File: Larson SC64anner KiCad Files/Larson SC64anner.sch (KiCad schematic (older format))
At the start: 67 parts, among them J1 Conn_02x03_Counter_Clockwise, J10 Conn_02x03_Counter_Clockwise, J11 Conn_02x03_Counter_Clockwise, J12 Conn_02x03_Counter_Clockwise, J13 Conn_02x03_Counter_Clockwise, J14 Conn_02x03_Counter_Clockwise, J15 Conn_02x03_Counter_Clockwise, J16 Conn_02x03_Counter_Clockwise, J17 Conn_02x03_Counter_Clockwise, J18 Conn_02x03_Counter_Clockwise, J19 Conn_02x03_Counter_Clockwise, J2 Conn_02x03_Counter_Clockwise, J20 Conn_02x03_Counter_Clockwise, J21 Conn_01x02, J3 Conn_02x03_Counter_Clockwise, J4 Conn_02x03_Counter_Clockwise, J5 Conn_02x03_Counter_Clockwise, J6 Conn_02x03_Counter_Clockwise, J7 Conn_02x03_Counter_Clockwise, J8 Conn_02x03_Counter_Clockwise, J9 Conn_02x03_Counter_Clockwise, U1 ATtiny85V-10PU

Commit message: no message
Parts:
- added C1, C2, C3: 10uF, Capacitor_THT:CP_Radial_D5.0mm_P2.50mm, symbol Device:CP
- added C4: 10nF, Capacitor_THT:C_Disc_D7.5mm_W2.5mm_P5.00mm, symbol Device:C
- added D1: 1N4148, Diode_THT:D_DO-35_SOD27_P7.62mm_Horizontal, symbol Diode:1N4148
- added J22, J27: 1x02, Connector_PinHeader_2.54mm:PinHeader_1x02_P2.54mm_Vertical, symbol Connector_Generic:Conn_01x02
- added J23, J24, J25, J26: 1x01, Connector_PinHeader_2.54mm:PinHeader_1x01_P2.54mm_Vertical, symbol Connector:Conn_01x01_Male
- added R26, R27: 10k Ohm, Resistor_THT:R_Axial_DIN0207_L6.3mm_D2.5mm_P2.54mm_Vertical, symbol Device:R
- added R28: 150 Ohm, Resistor_THT:R_Axial_DIN0207_L6.3mm_D2.5mm_P2.54mm_Vertical, symbol Device:R
- added R29: 10k Ohm linear, Connector_PinHeader_2.54mm:PinHeader_1x03_P2.54mm_Vertical, symbol Device:R_POT
- added U2: NE555, Package_DIP:DIP-8_W7.62mm, symbol Timer:NE555
- added U3: SN74LVC2GU04DCKR, https://www.ti.com/lit/ds/symlink/sn74lvc2gu04.pdf, symbol dk_Logic-Buffers-Drivers-Receivers-Transceivers:SN74LVC2G17DBVR_Discontinued
- J1, J10, J11, J12, J13, J14, J15, J16, J17, J18, J19, J2, J20, J3, J4, J5, J6, J7, J8, J9: value Conn_02x03_Counter_Clockwise -> 2x03; Category (none) -> Pin Header; DK_Datasheet_Link (none) -> https://www.digikey.de/product-detail/en/amphenol-icc-fci/6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; DK_Product_Page (none) -> https://www.digikey.de/product-detail/en/amphenol-icc-fci/6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; Family (none) -> LSC; Price (none) -> 0,3
- J21: value Conn_01x02 -> 1x02; Category (none) -> Pin Header; DK_Datasheet_Link (none) -> https://www.digikey.de/product-detail/en/te-connectivity-am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; DK_Product_Page (none) -> https://www.digikey.de/product-detail/en/te-connectivity-am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; Family (none) -> LSC; Price (none) -> 0,55
- LED1, LED10, LED11, LED12, LED13, LED14, LED15, LED16, LED17, LED18, LED19, LED2, LED20, LED3, LED4, LED5, LED6, LED7, LED8, LED9: Category (none) -> LED; DK_Datasheet_Link (none) -> https://www.digikey.de/product-detail/de/kingbright/WP154A4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; DK_Product_Page (none) -> https://www.digikey.de/product-detail/de/kingbright/WP154A4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; Family (none) -> LSC; Price (none) -> 1,74
- R1, R10, R11, R12, R13, R14, R15, R16, R17, R18, R19, R2, R20, R3, R4, R5, R6, R7, R8, R9: value 80 -> 80 Ohm; Category (none) -> Resistor; DK_Datasheet_Link (none) -> https://www.digikey.de/product-detail/en/vishay-dale/CMF608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; DK_Product_Page (none) -> https://www.digikey.de/product-detail/en/vishay-dale/CMF608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; Family (none) -> LSC; Price (none) -> 0,73
- R21, R22, R23, R24, R25: value 10 -> 10 Ohm; Category (none) -> Resistor; DK_Datasheet_Link (none) -> https://www.digikey.de/product-detail/en/bourns-inc/FW10A10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; DK_Product_Page (none) -> https://www.digikey.de/product-detail/en/bourns-inc/FW10A10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; Family (none) -> LSC; Price (none) -> 0,53
- U1: value ATtiny85V-10PU -> ATtiny85V-20PU; symbol MCU_Microchip_ATtiny:ATtiny85V-10PU -> MCU_Microchip_ATtiny:ATtiny85-20PU; Category (none) -> IC; DK_Datasheet_Link (none) -> https://www.digikey.com/product-detail/en/microchip-technol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; DK_Product_Page (none) -> https://www.digikey.de/product-detail/de/microchip-technolo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; Family (none) -> LSC; Price (none) -> 1,10
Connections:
- new net: C1.1, J22.1 (Pin_1), R26.2
- new net: C2.1, J22.2 (Pin_2), R27.2
- new net: C1.2, D1.1 (K), J23.1 (Pin_1), R26.1
- new net: C2.2, D1.2 (A), R27.1
- new net: R28.1, R29.1, R29.2, U2.7 (DIS)
- new net: J27.2 (Pin_2), R29.3, U2.4 (R), U2.8 (VCC), U3.5 (VCC)
- new net: C3.1, R28.2, U2.2 (TR), U2.6 (THR)
- new net: C3.2, C4.2, J25.1 (Pin_1), U2.1 (GND), U3.2 (GND)
- new net: U2.3 (Q), U3.1 (1A)
- new net: C4.1, U2.5 (CV)
- new net: U3.3 (2A), U3.6 (1Y)
- new net: J26.1 (Pin_1), U3.4 (2Y)
- new net: J24.1 (Pin_1), J27.1 (Pin_1)

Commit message: Add files via upload
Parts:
- removed J25: 1x01, Connector_PinHeader_2.54mm:PinHeader_1x01_P2.54mm_Vertical, symbol Connector:Conn_01x01_Male
- removed J27: 1x02, Connector_PinHeader_2.54mm:PinHeader_1x02_P2.54mm_Vertical, symbol Connector_Generic:Conn_01x02
- added J26: 1x01, Connector_PinHeader_2.54mm:PinHeader_1x01_P2.54mm_Vertical, symbol Connector:Conn_01x01_Male
- renumbered J26 to J25
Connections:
- net at R28.1, R29.2, U2.7 (DIS): now also R29.3; no longer R29.1
- net at U2.4 (R), U2.8 (VCC), U3.5 (VCC): now also J24.1 (Pin_1), R29.1; no longer R29.3
- net at C3.1, R28.2, U2.2 (TR)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: now also J26.1 (Pin_1)
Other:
- moved on the sheet: R29
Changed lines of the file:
@@
 F 8 "CPU Brake" H 20300 2050 50  0001 C CNN "Family"
 	1    20300 2050
-	0    1    1    0
+	0    -1   -1   0
 $EndComp
 $Comp
@@
 $EndComp
 $Comp
-L Connector:Conn_01x01_Male J26
+L Connector:Conn_01x01_Male J25
 U 1 1 5EA768C3
 P 18900 5150
-F 0 "J26" H 19008 5331 50  0000 C CNN
+F 0 "J25" H 19008 5331 50  0000 C CNN
 F 1 "1x01" H 19000 5250 50  0000 C CNN
 F 2 "Connector_PinHeader_2.54mm:PinHeader_1x01_P2.54mm_Vertical" H 18900 5150 50  0001 C CNN
@@
 $EndComp
 $Comp
-L Connector:Conn_01x01_Male J25
-U 1 1 5EAA3C5C
-P 22200 4500
-F 0 "J25" H 22308 4681 50  0000 C CNN
-F 1 "1x01" H 22300 4600 50  0000 C CNN
-F 2 "Connector_PinHeader_2.54mm:PinHeader_1x01_P2.54mm_Vertical" H 22200 4500 50  0001 C CNN
-F 3 "http://www.adam-tech.com/downloader.php?p=PH1-XX-UA.pdf" H 22200 4500 50  0001 C CNN
-F 4 "Pin Header" H 22200 4500 50  0001 C CNN "Category"
-F 5 "https://www.digikey.de/product-detail/en/adam-tech/PH1-01-UA/2057-PH1-01-UA-ND/9830231" H 22200 4500 50  0001 C CNN "DK_Datasheet_Link"
-F 6 "https://www.digikey.de/product-detail/en/adam-tech/PH1-01-UA/2057-PH1-01-UA-ND/9830231" H 22200 4500 50  0001 C CNN "DK_Product_Page"
-F 7 "0,09" H 22200 4500 50  0001 C CNN "Price"
-F 8 "CPU Brake" H 22200 4500 50  0001 C CNN "Family"
-	1    22200 4500
-	-1   0    0    1
-$EndComp
-$Comp
 L Device:C C4
 U 1 1 5EAB8B01
@@
 F 0 "C4" H 20415 4241 50  0000 L CNN
 F 1 "10nF" H 20415 4150 50  0000 L CNN
-F 2 "Capacitor_THT:C_Disc_D7.5mm_W2.5mm_P5.00mm" H 20415 4059 50  0000 L CNN
+F 2 "Capacitor_THT:C_Disc_D7.5mm_W2.5mm_P5.00mm" H 20415 4059 50  0001 L CNN
 F 3 "http://www.vishay.com/docs/28535/vy2series.pdf" H 20300 4150 50  0001 C CNN
 F 4 "https://www.digikey.de/product-detail/de/vishay-bc-components/VY2103M63Y5US63V0/BC2698-ND/2356836" H 20300 4150 50  0001 C CNN "DK_Datasheet_Link"
@@
 	1    0    0    -1
 $EndComp
-$Comp
-L Connector_Generic:Conn_01x02 J27
-U 1 1 5EAFC628
-P 18950 2350
-F 0 "J27" H 18868 2025 50  0000 C CNN
-F 1 "1x02" H 18868 2116 50  0001 C CNN
-F 2 "Connector_PinHeader_2.54mm:PinHeader_1x02_P2.54mm_Vertical" H 18950 2350 50  0001 C CNN
-F 3 "https://www.te.com/commerce/DocumentDelivery/DDEController?Action=srchrtrv&DocNm=146256&DocType=Customer+Drawing&DocLang=English" H 18950 2350 50  0001 C CNN
-F 4 "Pin Header" H 18950 2350 50  0001 C CNN "Category"
-F 5 "https://www.digikey.de/product-detail/en/te-connectivity-amp-connectors/5-146256-3/A121369-ND/1153559" H 18950 2350 50  0001 C CNN "DK_Datasheet_Link"
-F 6 "https://www.digikey.de/product-detail/en/te-connectivity-amp-connectors/5-146256-3/A121369-ND/1153559" H 18950 2350 50  0001 C CNN "DK_Product_Page"
-F 7 "0,55" H 18950 2350 50  0001 C CNN "Price"
-F 8 "CPU Brake" H 18950 2350 50  0001 C CNN "Family"
-	1    18950 2350
-	0    -1   -1   0
-$EndComp
-Wire Wire Line
-	18350 2600 18950 2600
-Wire Wire Line
-	18950 2600 18950 2550
-Wire Wire Line
-	19050 2550 19050 2600
-Wire Wire Line
-	19050 2600 19350 2600
 Wire Wire Line
 	19350 2600 19350 2050
 Wire Wire Line
 	19350 2050 20150 2050
-Wire Wire Line
-	20300 2200 20300 2250
 Wire Wire Line
 	20500 2350 20300 2350
@@
 Wire Wire Line
 	22300 5150 19100 5150
-Connection ~ 22000 4500
 Wire Wire Line
 	20450 2050 20500 2050
@@
 Wire Wire Line
 	20500 2250 20300 2250
-Connection ~ 20300 2250
 Wire Wire Line
 	20300 2250 20300 2350
@@
 	19700 3850 19700 3200
 Connection ~ 19700 3200
+Wire Wire Line
+	18350 2600 19350 2600
+Wire Wire Line
+	20300 1900 20500 1900
+Wire Wire Line
+	20500 1900 20500 2050
+Connection ~ 20500 2050
+$Comp
+L Connector:Conn_01x01_Male J26
+U 1 1 5E8C2806
+P 19250 4500
+F 0 "J26" H 19358 4681 50  0000 C CNN
+F 1 "1x01" H 19350 4600 50  0000 C CNN
+F 2 "Connector_PinHeader_2.54mm:PinHeader_1x01_P2.54mm_Vertical" H 19250 4500 50  0001 C CNN
+F 3 "http://www.adam-tech.com/downloader.php?p=PH1-XX-UA.pdf" H 19250 4500 50  0001 C CNN
+F 4 "Pin Header" H 19250 4500 50  0001 C CNN "Category"
+F 5 "https://www.digikey.de/product-detail/en/adam-tech/PH1-01-UA/2057-PH1-01-UA-ND/9830231" H 19250 4500 50  0001 C CNN "DK_Datasheet_Link"
+F 6 "https://www.digikey.de/product-detail/en/adam-tech/PH1-01-UA/2057-PH1-01-UA-ND/9830231" H 19250 4500 50  0001 C CNN "DK_Product_Page"
+F 7 "0,09" H 19250 4500 50  0001 C CNN "Price"
+F 8 "CPU Brake" H 19250 4500 50  0001 C CNN "Family"
+	1    19250 4500
+	1    0    0    -1
+$EndComp
 $EndSCHEMATC

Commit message: Updated PCB
- Touchups
- Added mono / stereo headphone amp circuitry
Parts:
- added C10, C6: 470uF, Capacitor_THT:CP_Radial_D5.0mm_P2.50mm, symbol Device:CP
- added C11, C5, C8, C9: 10uF, Capacitor_THT:CP_Radial_D5.0mm_P2.50mm, symbol Device:CP
- added C12, C7: 100nF, Capacitor_THT:C_Disc_D7.5mm_W2.5mm_P5.00mm, symbol Device:C
- added J29, J30, J31, J32, J33, J34, J35, J36, J38, J39: 1x01, Connector_PinHeader_2.54mm:PinHeader_1x01_P2.54mm_Vertical, symbol Connector:Conn_01x01_Male
- added R30, R32: 18k Ohm, Resistor_THT:R_Axial_DIN0207_L6.3mm_D2.5mm_P2.54mm_Vertical, symbol Device:R
- added R31, R33: 10 Ohm, Resistor_THT:R_Axial_DIN0207_L6.3mm_D2.5mm_P2.54mm_Vertical, symbol Device:R
- added U4, U5: LM386N-4_NOPB, digikey-footprints:DIP-8_W7.62mm, symbol dk_Linear-Amplifiers-Audio:LM386N-4_NOPB
- C4: Family CPU Brake -> AMP; Price 0,44 -> 0,28
- U3: footprint https://www.ti.com/lit/ds/symlink/sn74lvc2gu04.pdf -> Package_DIP:SMDIP-6_W7.62mm
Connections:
- net at J11.1 (Pin_1), J11.3 (Pin_3), J11.5 (Pin_5)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: now also J2.1 (Pin_1), J2.3 (Pin_3), J2.5 (Pin_5)
- new net: R30.1, U4.1 (Gain)
- new net: C5.1, R30.2
- new net: C5.2, C6.2, C7.1, J32.1 (Pin_1), J33.1 (Pin_1)
- new net: C8.1, U4.7 (BYPASS)
- new net: C11.2, C8.2, J30.1 (Pin_1), J34.1 (Pin_1), J39.1 (Pin_1), R31.1, R33.1, U4.2, U4.4 (GND), U5.2, U5.4 (GND)
- new net: C7.2, R31.2
- new net: C6.1, U4.5
- new net: J29.1 (Pin_1), U4.3
- new net: J31.1 (Pin_1), U4.6 (Vs)
- new net: R32.1, U5.1 (Gain)
- new net: C9.1, R32.2
- new net: C10.2, C12.1, C9.2, J38.1 (Pin_1)
- new net: C11.1, U5.7 (BYPASS)
- new net: C12.2, R33.2
- new net: C10.1, U5.5
- new net: J36.1 (Pin_1), U5.3
- new net: J35.1 (Pin_1), U5.6 (Vs)
- no-connect marks 1 -> 3
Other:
- moved on the sheet: C1, C2, C3, C4, D1, J1, J10, J11, J12, J13, J14, J15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

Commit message: Cleanup and documentation
- Deleted some unnecessary parts
- Started description on how to connect the headphone amp circuitry
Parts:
- removed J33, J34, J39: 1x01, Connector_PinHeader_2.54mm:PinHeader_1x01_P2.54mm_Vertical, symbol Connector:Conn_01x01_Male
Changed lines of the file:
@@
 	-1   0    0    1
 $EndComp
-$Comp
-L Connector:Conn_01x01_Male J34
-U 1 1 5ECDFA96
-P 12450 3550
-F 0 "J34" H 12558 3731 50  0000 C CNN
-F 1 "1x01" H 12550 3650 50  0001 C CNN
-F 2 "Connector_PinHeader_2.54mm:PinHeader_1x01_P2.54mm_Vertical" H 12450 3550 50  0001 C CNN
-F 3 "http://www.adam-tech.com/downloader.php?p=PH1-XX-UA.pdf" H 12450 3550 50  0001 C CNN
-F 4 "Pin Header" H 12450 3550 50  0001 C CNN "Category"
-F 5 "https://www.digikey.de/product-detail/en/adam-tech/PH1-01-UA/2057-PH1-01-UA-ND/9830231" H 12450 3550 50  0001 C CNN "DK_Datasheet_Link"
-F 6 "https://www.digikey.de/product-detail/en/adam-tech/PH1-01-UA/2057-PH1-01-UA-ND/9830231" H 12450 3550 50  0001 C CNN "DK_Product_Page"
-F 7 "0,09" H 12450 3550 50  0001 C CNN "Price"
-F 8 "AMP" H 12450 3550 50  0001 C CNN "Family"
-	1    12450 3550
-	-1   0    0    1
-$EndComp
-Wire Wire Line
-	11750 2600 12000 2600
-Wire Wire Line
-	12250 3550 12150 3550
 Wire Wire Line
 	11750 3550 11750 3400
-$Comp
-L Connector:Conn_01x01_Male J33
-U 1 1 5ED7B605
-P 12450 2450
-F 0 "J33" H 12558 2631 50  0000 C CNN
-F 1 "1x01" H 12550 2550 50  0001 C CNN
-F 2 "Connector_PinHeader_2.54mm:PinHeader_1x01_P2.54mm_Vertical" H 12450 2450 50  0001 C CNN
-F 3 "http://www.adam-tech.com/downloader.php?p=PH1-XX-UA.pdf" H 12450 2450 50  0001 C CNN
-F 4 "Pin Header" H 12450 2450 50  0001 C CNN "Category"
-F 5 "https://www.digikey.de/product-detail/en/adam-tech/PH1-01-UA/2057-PH1-01-UA-ND/9830231" H 12450 2450 50  0001 C CNN "DK_Datasheet_Link"
-F 6 "https://www.digikey.de/product-detail/en/adam-tech/PH1-01-UA/2057-PH1-01-UA-ND/9830231" H 12450 2450 50  0001 C CNN "DK_Product_Page"
-F 7 "0,09" H 12450 2450 50  0001 C CNN "Price"
-F 8 "AMP" H 12450 2450 50  0001 C CNN "Family"
-	1    12450 2450
-	-1   0    0    1
-$EndComp
-Wire Wire Line
-	12250 2450 12000 2450
-Wire Wire Line
-	12000 2450 12000 2600
-Connection ~ 12000 2600
-Wire Wire Line
-	12000 2600 12250 2600
 $Comp
 L Device:R R32
@@
 	-1   0    0    1
 $EndComp
-$Comp
-L Connector:Conn_01x01_Male J39
-U 1 1 5EDD7B56
-P 12450 5450
-F 0 "J39" H 12558 5631 50  0000 C CNN
-F 1 "1x01" H 12550 5550 50  0001 C CNN
-F 2 "Connector_PinHeader_2.54mm:PinHeader_1x01_P2.54mm_Vertical" H 12450 5450 50  0001 C CNN
-F 3 "http://www.adam-tech.com/downloader.php?p=PH1-XX-UA.pdf" H 12450 5450 50  0001 C CNN
-F 4 "Pin Header" H 12450 5450 50  0001 C CNN "Category"
-F 5 "https://www.digikey.de/product-detail/en/adam-tech/PH1-01-UA/2057-PH1-01-UA-ND/9830231" H 12450 5450 50  0001 C CNN "DK_Datasheet_Link"
-F 6 "https://www.digikey.de/product-detail/en/adam-tech/PH1-01-UA/2057-PH1-01-UA-ND/9830231" H 12450 5450 50  0001 C CNN "DK_Product_Page"
-F 7 "0,09" H 12450 5450 50  0001 C CNN "Price"
-F 8 "AMP" H 12450 5450 50  0001 C CNN "Family"
-	1    12450 5450
-	-1   0    0    1
-$EndComp
-Wire Wire Line
-	12250 5450 12150 5450
 Wire Wire Line
 	11750 5450 11750 5300
@@
 Wire Wire Line
 	12150 5450 12150 3550
-Connection ~ 12150 5450
 Wire Wire Line
 	12150 5450 11750 5450
-Connection ~ 12150 3550
 Wire Wire Line
 	12150 3550 11750 3550
@@
 Connection ~ 11750 5450
 Connection ~ 10200 5350
+Wire Wire Line
+	11750 2600 12250 2600
 $EndSCHEMATC

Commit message: Updated PCB, README, Schmetic
Simpliefied things a bit.
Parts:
- removed J26, J30: 1x01, Connector_PinHeader_2.54mm:PinHeader_1x01_P2.54mm_Vertical, symbol Connector:Conn_01x01_Male
- added J26: 2x05, Connector_PinHeader_2.54mm:PinHeader_2x05_P2.54mm_Vertical, symbol Connector_Generic:Conn_02x05_Top_Bottom
- J21: DK_Datasheet_Link https://www.digikey.de/product-detail/en/te-connectivity-am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 -> (none)
- R1, R10, R11, R12, R13, R14, R15, R16, R17, R18, R19, R2, R20, R21, R22, R23, R24, R25, R26, R27, R28, R3, R30, R31, R32, R33, R4, R5, R6, R7, R8, R9: footprint Resistor_THT:R_Axial_DIN0207_L6.3mm_D2.5mm_P2.54mm_Vertical -> libraries:R_Axial_DIN0207_L6.3mm_D2.5mm_P2.54mm_Vertical_reduced_courtyard
- U4, U5: footprint digikey-footprints:DIP-8_W7.62mm -> Package_DIP:DIP-8_W7.62mm
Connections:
- net at U1.4 (GND): now also C11.2, C3.1, C8.2, R28.2, R31.1, R33.1, U2.2 (TR), U2.6 (THR), U4.2, U4.4 (GND), U5.2, U5.4 (GND), J26.1 (Pin_1), J26.10 (Pin_10), J26.2 (Pin_2), J26.3 (Pin_3), J26.4 (Pin_4), J26.5 (Pin_5), J26.6 (Pin_6), J26.7 (Pin_7), J26.8 (Pin_8), J26.9 (Pin_9); no longer J21.1 (Pin_1)
- net at J21.2 (Pin_2), U1.8 (VCC): now also J21.1 (Pin_1)
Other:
- note added: "CPU Brake"
- note added: "Headphone Amp"
- note added: "Larson Scanner"
- note added: "Reset Button"

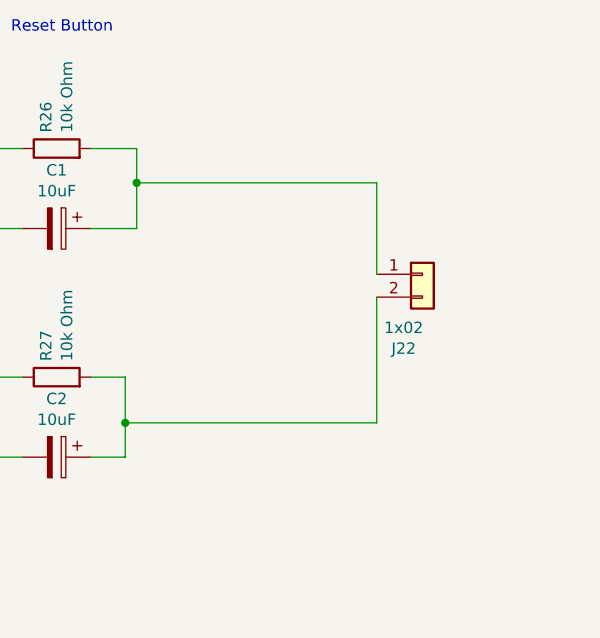
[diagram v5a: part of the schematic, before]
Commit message: Updated README
Switched the description of the connections from stupid text lists to tables. Much better!
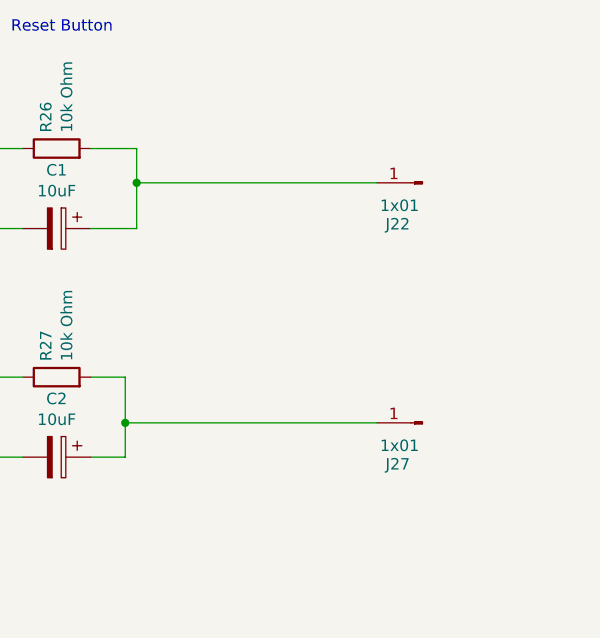
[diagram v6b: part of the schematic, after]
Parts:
- removed J22: 1x02, Connector_PinHeader_2.54mm:PinHeader_1x02_P2.54mm_Vertical, symbol Connector_Generic:Conn_01x02
- added J22, J27: 1x01, Connector_PinHeader_2.54mm:PinHeader_1x01_P2.54mm_Vertical, symbol Connector:Conn_01x01_Male
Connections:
- net at C1.1, R26.2: now also J22.1 (Pin_1)
- net at C2.1, R27.2: now also J27.1 (Pin_1)
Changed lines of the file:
@@
-$EndComp
-$Comp
-L Connector_Generic:Conn_01x02 J22
-U 1 1 5E7B9A5D
-P 20150 9950
-F 0 "J22" H 20068 9625 50  0000 C CNN
-F 1 "1x02" H 20068 9716 50  0000 C CNN
-F 2 "Connector_PinHeader_2.54mm:PinHeader_1x02_P2.54mm_Vertical" H 20150 9950 50  0001 C CNN
-F 3 "https://www.te.com/commerce/DocumentDelivery/DDEController?Action=srchrtrv&DocNm=146256&DocType=Customer+Drawing&DocLang=English" H 20150 9950 50  0001 C CNN
-F 4 "Pin Header" H 20150 9950 50  0001 C CNN "Category"
-F 5 "https://www.digikey.de/product-detail/en/te-connectivity-amp-connectors/5-146256-3/A121369-ND/1153559" H 20150 9950 50  0001 C CNN "DK_Datasheet_Link"
-F 6 "https://www.digikey.de/product-detail/en/te-connectivity-amp-connectors/5-146256-3/A121369-ND/1153559" H 20150 9950 50  0001 C CNN "DK_Product_Page"
-F 7 "0,55" H 20150 9950 50  0001 C CNN "Price"
-F 8 "Reset" H 20150 9950 50  0001 C CNN "Family"
-	1    20150 9950
-	1    0    0    -1
 $EndComp
 $Comp
@@
 	18850 10400 18700 10400
 Wire Wire Line
-	19950 9950 19950 9550
-Wire Wire Line
 	19950 9550 18900 9550
 Connection ~ 18900 9550
 Wire Wire Line
 	18900 9550 18900 9750
-Wire Wire Line
-	19950 10050 19950 10600
 Wire Wire Line
 	19950 10600 18850 10600
@@
 Wire Wire Line
 	1000 11250 1000 10800
+$Comp
+L Connector:Conn_01x01_Male J22
+U 1 1 5E89EC9C
+P 20150 9550
+F 0 "J22" H 20258 9731 50  0000 C CNN
+F 1 "1x01" H 20250 9650 50  0000 C CNN
+F 2 "Connector_PinHeader_2.54mm:PinHeader_1x01_P2.54mm_Vertical" H 20150 9550 50  0001 C CNN
+F 3 "http://www.adam-tech.com/downloader.php?p=PH1-XX-UA.pdf" H 20150 9550 50  0001 C CNN
+F 4 "Pin Header" H 20150 9550 50  0001 C CNN "Category"
+F 5 "https://www.digikey.de/product-detail/en/adam-tech/PH1-01-UA/2057-PH1-01-UA-ND/9830231" H 20150 9550 50  0001 C CNN "DK_Datasheet_Link"
+F 6 "https://www.digikey.de/product-detail/en/adam-tech/PH1-01-UA/2057-PH1-01-UA-ND/9830231" H 20150 9550 50  0001 C CNN "DK_Product_Page"
+F 7 "0,09" H 20150 9550 50  0001 C CNN "Price"
+F 8 "CPU Brake" H 20150 9550 50  0001 C CNN "Family"
+	1    20150 9550
+	-1   0    0    1
+$EndComp
+$Comp
+L Connector:Conn_01x01_Male J27
+U 1 1 5E8CA135
+P 20150 10600
+F 0 "J27" H 20258 10781 50  0000 C CNN
+F 1 "1x01" H 20250 10700 50  0000 C CNN
+F 2 "Connector_PinHeader_2.54mm:PinHeader_1x01_P2.54mm_Vertical" H 20150 10600 50  0001 C CNN
+F 3 "http://www.adam-tech.com/downloader.php?p=PH1-XX-UA.pdf" H 20150 10600 50  0001 C CNN
+F 4 "Pin Header" H 20150 10600 50  0001 C CNN "Category"
+F 5 "https://www.digikey.de/product-detail/en/adam-tech/PH1-01-UA/2057-PH1-01-UA-ND/9830231" H 20150 10600 50  0001 C CNN "DK_Datasheet_Link"
+F 6 "https://www.digikey.de/product-detail/en/adam-tech/PH1-01-UA/2057-PH1-01-UA-ND/9830231" H 20150 10600 50  0001 C CNN "DK_Product_Page"
+F 7 "0,09" H 20150 10600 50  0001 C CNN "Price"
+F 8 "CPU Brake" H 20150 10600 50  0001 C CNN "Family"
+	1    20150 10600
+	-1   0    0    1
+$EndComp
 $EndSCHEMATC
